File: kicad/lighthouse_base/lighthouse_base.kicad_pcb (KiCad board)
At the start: 2 copper layers, 0 parts

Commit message: started with pcb lighthouse_base
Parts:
- added BT1: Battery_Cell, Connector_PinHeader_2.54mm:PinHeader_1x02_P2.54mm_Vertical, F.Cu at (41.6, 130.1)
- added BT2: Keystone 3002, Battery:BatteryHolder_Keystone_3002_1x2032, F.Cu at (146.0, 62.2)
- added C1: 10uF, Capacitor_SMD:C_0805_2012Metric_Pad1.18x1.45mm_HandSolder, F.Cu at (66.6, 78.8)
- added C10: 100nF, Capacitor_SMD:C_0603_1608Metric_Pad1.08x0.95mm_HandSolder, F.Cu at (88.0, 79.6)
- added C11: 100nF, Capacitor_SMD:C_0603_1608Metric_Pad1.08x0.95mm_HandSolder, F.Cu at (88.0, 81.4)
- added C12: 10uF, Capacitor_SMD:C_0805_2012Metric_Pad1.18x1.45mm_HandSolder, F.Cu at (97.8, 102.2)
- added C13: 100nF, Capacitor_SMD:C_0603_1608Metric_Pad1.08x0.95mm_HandSolder, F.Cu at (103.1, 102.2)
- added C14: 100nF, Capacitor_SMD:C_0603_1608Metric_Pad1.08x0.95mm_HandSolder, F.Cu at (114.7, 79.8)
- added C2: 10uF, Capacitor_SMD:C_0805_2012Metric_Pad1.18x1.45mm_HandSolder, F.Cu at (74.1, 82.9)
- added C3: 10uF, Capacitor_SMD:C_0805_2012Metric_Pad1.18x1.45mm_HandSolder, F.Cu at (54.9, 125.2)
- added C4: 10uF, Capacitor_SMD:C_0805_2012Metric_Pad1.18x1.45mm_HandSolder, F.Cu at (73.4, 140.1)
- added C5: 10uF, Capacitor_SMD:C_0805_2012Metric_Pad1.18x1.45mm_HandSolder, F.Cu at (52.5, 108.3)
- added C6: 10nF, Capacitor_SMD:C_0603_1608Metric_Pad1.08x0.95mm_HandSolder, F.Cu at (64.2, 139.4)
- added C7: 10uF, Capacitor_SMD:C_0603_1608Metric_Pad1.08x0.95mm_HandSolder, F.Cu at (88.0, 74.4)
- added C8: 100nF, Capacitor_SMD:C_0603_1608Metric_Pad1.08x0.95mm_HandSolder, F.Cu at (88.0, 76.1)
- added C9: 100nF, Capacitor_SMD:C_0603_1608Metric_Pad1.08x0.95mm_HandSolder, F.Cu at (88.0, 77.9)
- added D1: B130-13-F, Diode_SMD:D_SMA_Handsoldering, F.Cu at (73.9, 89.9)
- added D2: DF2S16FS, Diode_SMD:D_SOD-523, F.Cu at (54.8, 86.0)
- added D3: B130-13-F, Diode_SMD:D_SMA_Handsoldering, F.Cu at (57.7, 103.3)
- added D4: PRTR5V0U2X, Package_TO_SOT_SMD:SOT-143, F.Cu at (56.9, 97.4)
- added D5: PMEG4002EJ, Diode_SMD:D_SOD-323F, F.Cu at (127.3, 63.4)
- added J1: Barrel_Jack_Switch, Connector_BarrelJack:BarrelJack_CUI_PJ-063AH_Horizontal, F.Cu at (52.4, 85.5)
- added J2: USB_C_Receptacle_USB2.0_14P, Connector_USB:USB_C_Receptacle_GCT_USB4110, F.Cu at (43.7, 99.3)
- added J3: Conn_01x07, Connector_PinHeader_1.27mm:PinHeader_1x07_P1.27mm_Vertical, F.Cu at (114.5, 112.3)
- added J4: Conn_01x12, Connector_Molex:Molex_Picoflex_90325-0012_2x06_P1.27mm_Vertical, F.Cu at (66.8, 110.6)
- added J5: Conn_01x12, Connector_Molex:Molex_Picoflex_90325-0012_2x06_P1.27mm_Vertical, F.Cu at (71.2, 54.9)
- added J6: Conn_01x06, Connector_Molex:Molex_Picoflex_90325-0006_2x03_P1.27mm_Vertical, F.Cu at (119.5, 54.4)
- added J7: Conn_01x02, Connector_PinHeader_2.54mm:PinHeader_1x02_P2.54mm_Vertical, F.Cu at (53.0, 51.3)
- added J8: Conn_01x05, Connector_PinHeader_1.27mm:PinHeader_1x05_P1.27mm_Vertical, F.Cu at (160.1, 70.2)
- added JP1: Jumper_3_Bridged12, Jumper:SolderJumper-3_P1.3mm_Bridged2Bar12_RoundedPad1.0x1.5mm, F.Cu at (46.5, 68.3)
- added Q1: DMP3099L, Package_TO_SOT_SMD:SOT-23-3, F.Cu at (57.6, 85.7)
- added R1: 1M, Resistor_SMD:R_0603_1608Metric_Pad0.98x0.95mm_HandSolder, F.Cu at (64.2, 142.9)
- added R10: 0R, Resistor_SMD:R_0603_1608Metric_Pad0.98x0.95mm_HandSolder, F.Cu at (96.0, 89.2)
- added R11: 1M, Resistor_SMD:R_0603_1608Metric_Pad0.98x0.95mm_HandSolder, F.Cu at (98.5, 89.2)
- added R12: 1M, Resistor_SMD:R_0603_1608Metric_Pad0.98x0.95mm_HandSolder, F.Cu at (101.0, 89.2)
- added R13: 4k7, Resistor_SMD:R_0603_1608Metric_Pad0.98x0.95mm_HandSolder, F.Cu at (107.0, 77.1)
- added R14: 4k7, Resistor_SMD:R_0603_1608Metric_Pad0.98x0.95mm_HandSolder, F.Cu at (107.0, 79.6)
- added R15: 10k, Resistor_SMD:R_0603_1608Metric_Pad0.98x0.95mm_HandSolder, F.Cu at (91.2, 71.5)
- added R2: 10k, Resistor_SMD:R_0603_1608Metric_Pad0.98x0.95mm_HandSolder, F.Cu at (59.5, 121.4)
- added R3: 22R, Resistor_SMD:R_0603_1608Metric_Pad0.98x0.95mm_HandSolder, F.Cu at (66.9, 96.6)
- added R4: 22R, Resistor_SMD:R_0603_1608Metric_Pad0.98x0.95mm_HandSolder, F.Cu at (66.9, 99.2)
- added R5: 5k1, Resistor_SMD:R_0603_1608Metric_Pad0.98x0.95mm_HandSolder, F.Cu at (62.4, 96.6)
- added R6: 5k1, Resistor_SMD:R_0603_1608Metric_Pad0.98x0.95mm_HandSolder, F.Cu at (62.4, 99.1)
- added R7: 0R, Resistor_SMD:R_0603_1608Metric_Pad0.98x0.95mm_HandSolder, F.Cu at (62.4, 73.2)
- added R8: 0R, Resistor_SMD:R_0603_1608Metric_Pad0.98x0.95mm_HandSolder, F.Cu at (62.4, 75.7)
- added R9: 0R, Resistor_SMD:R_0603_1608Metric_Pad0.98x0.95mm_HandSolder, F.Cu at (93.5, 89.2)
- added SW1: ~, lighthouse:PTS526, B.Cu at (130.4, 108.5)
- added TP1: TestPoint, TestPoint:TestPoint_Pad_D1.5mm, F.Cu at (101.7, 33.5)
- added TP10: TestPoint, TestPoint:TestPoint_Pad_D1.5mm, F.Cu at (108.8, 30.0)
- added TP11: TestPoint, TestPoint:TestPoint_Pad_D1.5mm, F.Cu at (112.3, 30.0)
- added TP12: TestPoint, TestPoint:TestPoint_Pad_D1.5mm, F.Cu at (115.9, 30.0)
- added TP13: TestPoint, TestPoint:TestPoint_Pad_D1.5mm, F.Cu at (119.4, 30.0)
- added TP14: TestPoint, TestPoint:TestPoint_Pad_D1.5mm, F.Cu at (101.7, 26.4)
- added TP15: TestPoint, TestPoint:TestPoint_Pad_D1.5mm, F.Cu at (105.2, 26.4)
- added TP16: TestPoint, TestPoint:TestPoint_Pad_D1.5mm, F.Cu at (108.8, 26.4)
- added TP17: TestPoint, TestPoint:TestPoint_Pad_D1.5mm, F.Cu at (112.3, 26.4)
- added TP18: TestPoint, TestPoint:TestPoint_Pad_D1.5mm, F.Cu at (115.9, 26.4)
- added TP19: TestPoint, TestPoint:TestPoint_Pad_D1.5mm, F.Cu at (119.4, 26.4)
- added TP2: TestPoint, TestPoint:TestPoint_Pad_D1.5mm, F.Cu at (105.2, 33.5)
- added TP20: TestPoint, TestPoint:TestPoint_Pad_D1.5mm, F.Cu at (125.4, 22.6)
- added TP21: TestPoint, TestPoint:TestPoint_Pad_D1.5mm, F.Cu at (125.4, 26.1)
- added TP22: TestPoint, TestPoint:TestPoint_Pad_D1.5mm, F.Cu at (125.4, 29.7)
- added TP23: TestPoint, TestPoint:TestPoint_Pad_D1.5mm, F.Cu at (125.4, 33.2)
- added TP24: TestPoint, TestPoint:TestPoint_Pad_D1.5mm, F.Cu at (125.4, 36.8)
- added TP3: TestPoint, TestPoint:TestPoint_Pad_D1.5mm, F.Cu at (108.8, 33.5)
- added TP4: TestPoint, TestPoint:TestPoint_Pad_D1.5mm, F.Cu at (112.3, 33.5)
- added TP5: TestPoint, TestPoint:TestPoint_Pad_D1.5mm, F.Cu at (115.9, 33.5)
- added TP7: TestPoint, TestPoint:TestPoint_Pad_D1.5mm, F.Cu at (119.4, 33.5)
- added TP8: TestPoint, TestPoint:TestPoint_Pad_D1.5mm, F.Cu at (101.7, 30.0)
- added TP9: TestPoint, TestPoint:TestPoint_Pad_D1.5mm, F.Cu at (105.2, 30.0)
- added U1: R-78E5.0-1.0, Converter_DCDC:Converter_DCDC_RECOM_R-78E-0.5_THT, F.Cu at (63.4, 87.3)
- added U2: MCP73831-2-OT, Package_TO_SOT_SMD:SOT-23-5, F.Cu at (64.3, 120.1)
- added U3: TLV75533PDBV, Package_TO_SOT_SMD:SOT-23-5, F.Cu at (70.2, 140.0)
- added U4: MCP111T-xxxE_TT, Package_TO_SOT_SMD:SOT-23-3, F.Cu at (60.7, 141.5)
- added U5: STM32L412R8Tx, Package_QFP:LQFP-64_10x10mm_P0.5mm, F.Cu at (97.7, 79.3)
- added U6: AT25SF081-SSHD-X, Package_SO:SOIC-8_3.9x4.9mm_P1.27mm, F.Cu at (96.7, 96.6)
- added U7: RV-3028-C7, Package_SON:MicroCrystal_C7_SON-8_1.5x3.2mm_P0.9mm, F.Cu at (111.0, 79.4)
- added U8: ~, lighthouse:DFPlayer_Mini-TF-16P, F.Cu at (50.1, 66.8)
- added U9: ~, lighthouse:BC805M, F.Cu at (158.1, 79.0)
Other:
- board text added: "Backlight"
- board text added: "Buttons"
- board text added: "Front Display"

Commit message: lighthouse base rev 1 done
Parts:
- removed TP19, TP20, TP5, TP7, TP8, TP9: TestPoint, TestPoint:TestPoint_Pad_D1.5mm
- added J10: Conn_01x07, Connector_PinHeader_2.54mm:PinHeader_1x07_P2.54mm_Vertical, F.Cu at (76.8, 109.0)
- added J9: Conn_01x04, Connector_PinHeader_2.54mm:PinHeader_1x04_P2.54mm_Vertical, F.Cu at (76.8, 112.0)
- C7: footprint Capacitor_SMD:C_0603_1608Metric_Pad1.08x0.95mm_HandSolder -> Capacitor_SMD:C_0805_2012Metric_Pad1.18x1.45mm_HandSolder
- TP1, TP10, TP11, TP12, TP13, TP14, TP15, TP16, TP17, TP18, TP2, TP21, TP22, TP23, TP24, TP3, TP4: footprint TestPoint:TestPoint_Pad_D1.5mm -> TestPoint:TestPoint_Pad_D1.0mm
- moved J8 66.2 mm to (109.6, 113.0)
- moved TP21 63.0 mm to (100.9, 84.1)
- moved TP22 56.9 mm to (103.4, 82.2)
- moved TP16 53.9 mm to (83.1, 73.8)
- moved TP13 53.8 mm to (87.3, 73.2)
- moved TP23 52.5 mm to (105.4, 81.7)
- moved TP14 49.6 mm to (85.1, 73.2)
- moved U4 49.0 mm to (74.8, 94.6)
- moved TP18 47.8 mm to (91.8, 67.7)
- moved TP2 47.7 mm to (83.1, 75.8)
- moved C4 47.6 mm to (83.6, 93.6)
- moved U3 47.6 mm to (80.5, 93.5)
- moved TP24 47.3 mm to (105.4, 79.6)
- moved R1 47.0 mm to (74.8, 97.1), turned to 0 degrees
- moved C6 46.7 mm to (77.6, 94.6)
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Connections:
- net SPI_SCLK renamed SPI1_SCLK
- U5 pad 11: Net-(U5-PC3) -> unconnected-(U5-PC3-Pad11)
- U5 pad 29: Net-(U5-PB10) -> unconnected-(U5-PB10-Pad29)
- U5 pad 30: Net-(U5-PB11) -> unconnected-(U5-PB11-Pad30)
- U5 pad 40: Net-(U5-PC9) -> unconnected-(U5-PC9-Pad40)
- U5 pad 41: Net-(U5-PA8) -> ~{SPI1_CS1}
- U5 pad 50: Net-(U5-PA15) -> ~{SPI1_CS2}
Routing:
- net +3.3V: track 0.00 -> 338.6 mm, vias 0 -> 9
- net I2C1_SDA: track 0.00 -> 166.9 mm, vias 0 -> 3
- net I2C1_SCL: track 0.00 -> 163.8 mm, vias 0 -> 4
- net ~{IS_INTB}: track 0.00 -> 129.3 mm, vias 0 -> 3
- net ~{IS_SDB}: track 0.00 -> 126.9 mm, vias 0 -> 3
- net GND: track 0.00 -> 125.9 mm, vias 0 -> 15
- net +5V: track 0.00 -> 83.4 mm, vias 0 -> 2
- net +12V: track 0.00 -> 70.2 mm, vias 0 -> 1
- net ~{STM_RST}: track 0.00 -> 67.9 mm, vias 0 -> 3
- net USB_D-: track 0.00 -> 64.2 mm, vias 0 -> 2
- net USB_D+: track 0.00 -> 64.2 mm, vias 0 -> 2
- net BTN1: track 0.00 -> 53.7 mm, vias 0 -> 2
- net WHITE_PWM2: track 0.00 -> 52.5 mm, vias 0 -> 2
- net ~{SPI1_CS2}: track 0.00 -> 52.5 mm, vias 0 -> 2
- net Net-(BT2-+): track 0.00 -> 52.1 mm
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- added copper zone on In2.Cu, net GND
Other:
- board outline added: 90 x 66.3 mm
- copper layers 2 -> 4
- board text added: "lighthouse base rev1 MEgli 2024-11-06"

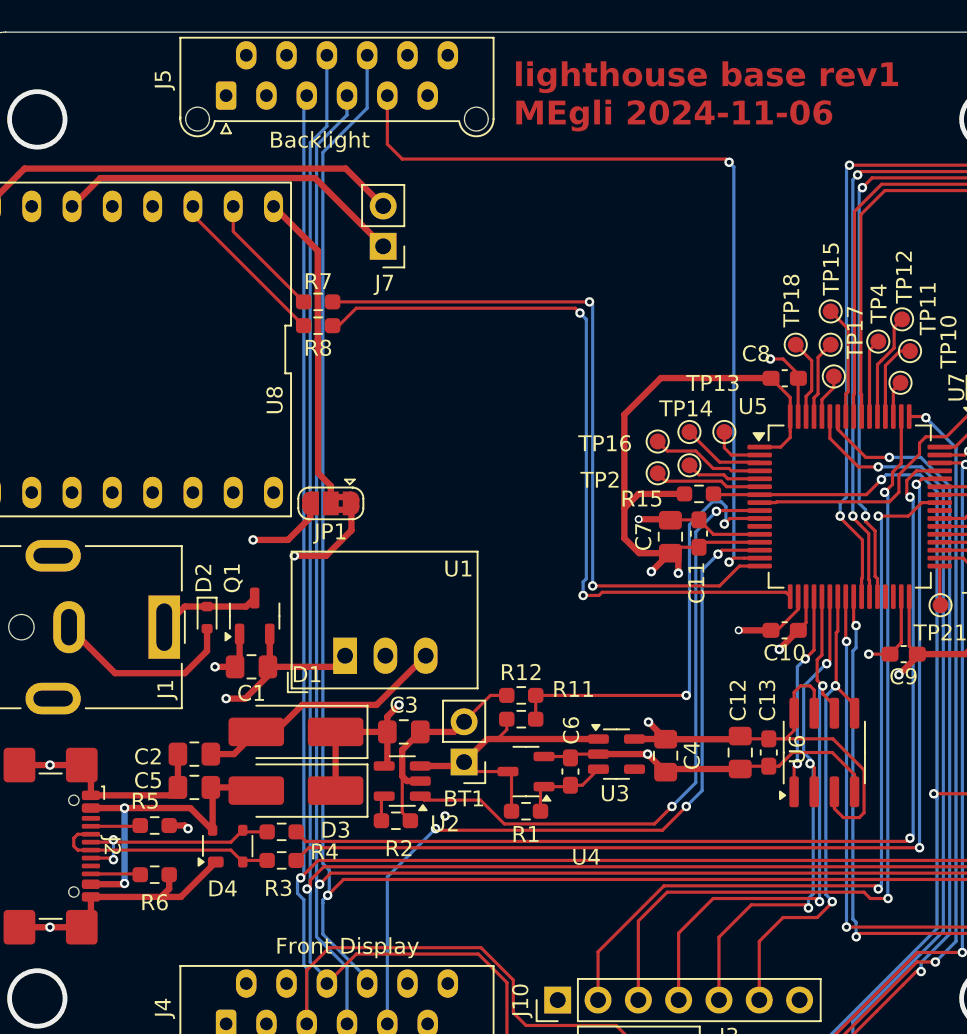
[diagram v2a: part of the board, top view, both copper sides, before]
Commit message: rev1: added 32 kHz XTAL, interrupt signals for VBUS + +5V, ... many more
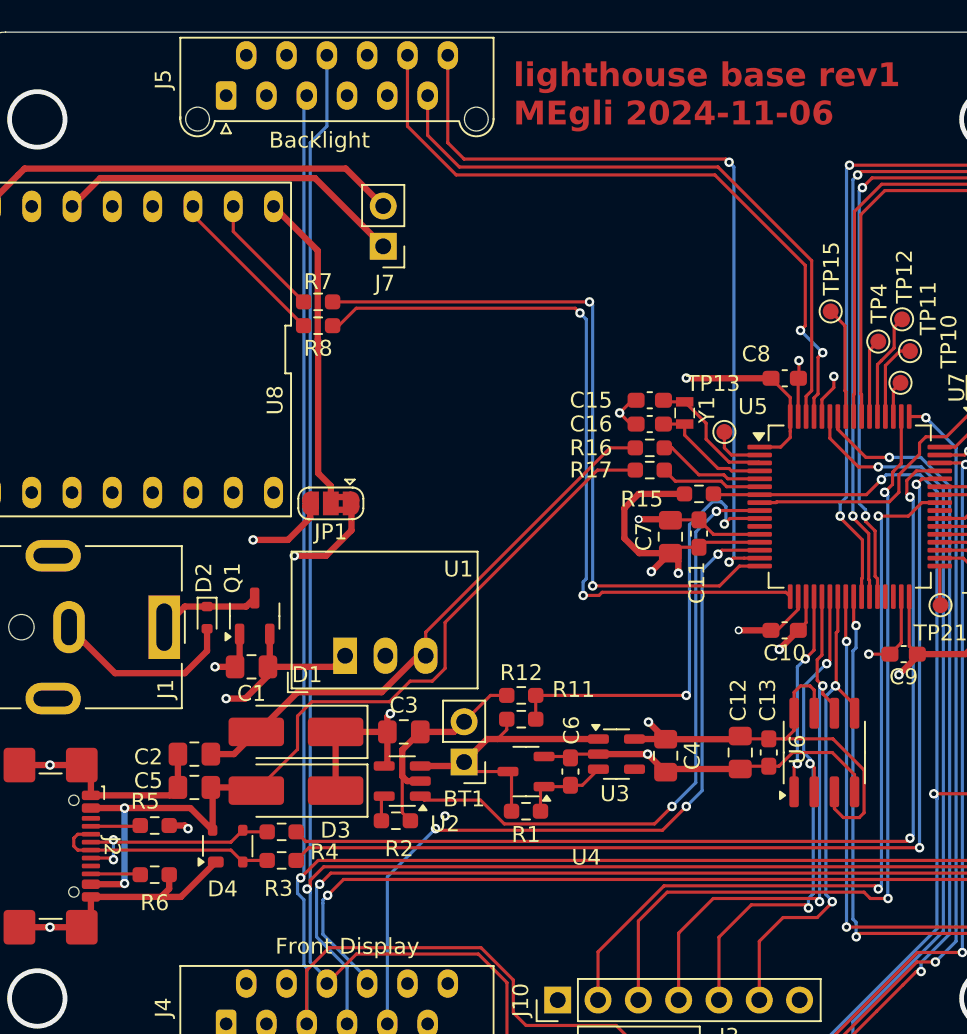
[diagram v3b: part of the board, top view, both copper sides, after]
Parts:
- removed TP1, TP14, TP16, TP17, TP18, TP2, TP3: TestPoint, TestPoint:TestPoint_Pad_D1.0mm
- added C15: 12.5pF, Capacitor_SMD:C_0603_1608Metric_Pad1.08x0.95mm_HandSolder, F.Cu at (82.6, 71.2)
- added C16: 12.5pF, Capacitor_SMD:C_0603_1608Metric_Pad1.08x0.95mm_HandSolder, F.Cu at (82.6, 72.7)
- added R16: 1k, Resistor_SMD:R_0603_1608Metric_Pad0.98x0.95mm_HandSolder, F.Cu at (82.6, 74.2)
- added R17: 1k, Resistor_SMD:R_0603_1608Metric_Pad0.98x0.95mm_HandSolder, F.Cu at (82.6, 75.6)
- added Y1: 9HT11-32.768KDZB-T, Lighthouse1:9HT1132768KDZBT, F.Cu at (84.8, 72.0)
- U5: value STM32L412R8Tx -> STM32L412RBTx
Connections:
- net Net-(D1-A) renamed +5VA
- J4 pad 7: ~{IS_SDB} -> ~{IS_SDB1}
- J4 pad 8: ~{IS_INTB} -> ~{IS_INTB1}
- J5 pad 10: unconnected-(J5-Pin_10-Pad10) -> ~{IS_SDB2}
- J5 pad 11: unconnected-(J5-Pin_11-Pad11) -> ~{IS_INTB2}
- J5 pad 12: unconnected-(J5-Pin_12-Pad12) -> WHITE_PWM2
- J5 pad 7: ~{IS_SDB} -> unconnected-(J5-Pin_7-Pad7)
- J5 pad 8: ~{IS_INTB} -> unconnected-(J5-Pin_8-Pad8)
- J5 pad 9: WHITE_PWM2 -> unconnected-(J5-Pin_9-Pad9)
- U5 pad 37: ~{IS_SDB} -> ~{IS_SDB1}
- U5 pad 38: ~{IS_INTB} -> ~{IS_INTB1}
- U5 pad 60: Net-(U5-PH3) -> GND
- U5 pad 61: Net-(U5-PB8) -> ~{IS_SDB2}
- U5 pad 62: Net-(U5-PB9) -> ~{IS_INTB2}
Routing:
- net ~{IS_INTB}: track 129.3 -> 0.00 mm, vias 3 -> 0
- net ~{IS_SDB}: track 126.9 -> 0.00 mm, vias 3 -> 0
- net ~{IS_SDB1}: track 0.00 -> 76.2 mm, vias 0 -> 3
- net ~{IS_INTB1}: track 0.00 -> 75.1 mm, vias 0 -> 3
- net ~{IS_SDB2}: track 0.00 -> 43.6 mm, vias 0 -> 2
- net ~{IS_INTB2}: track 0.00 -> 39.9 mm
- net VBUS: track 20.9 -> 56.1 mm
- net +5VA: track 16.1 -> 35.6 mm
- net Net-(U5-PB9): track 5.09 -> 0.00 mm
- net Net-(U5-PB8): track 4.96 -> 0.00 mm
- net GND: track 125.9 -> 130.1 mm, vias 15 -> 17
- net Net-(U5-PC14): track 5.23 -> 8.28 mm
- net Net-(U5-PH3): track 2.84 -> 0.00 mm
- net Net-(U5-PH0): track 4.78 -> 6.82 mm
- net +3.3V: track 338.6 -> 340.4 mm, vias 9 -> 10
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
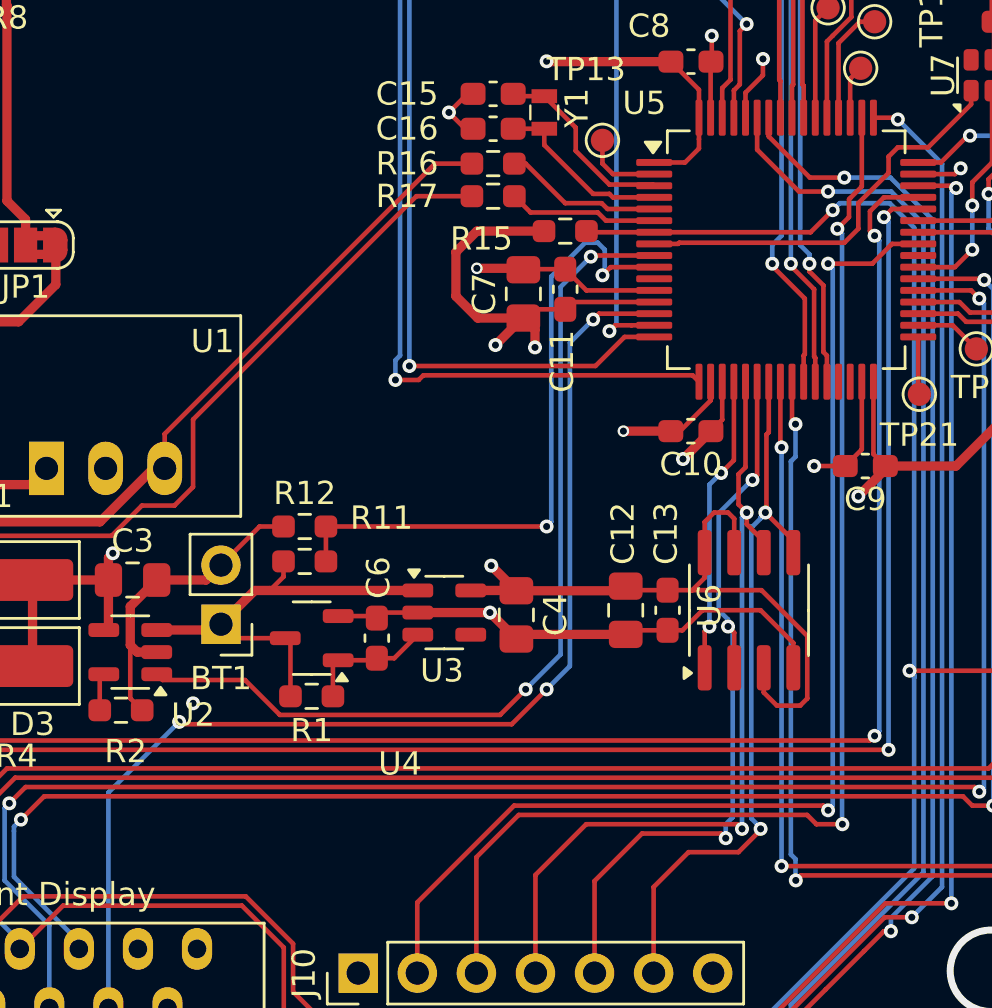
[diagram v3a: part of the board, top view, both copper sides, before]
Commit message: ordererd lighthouse display
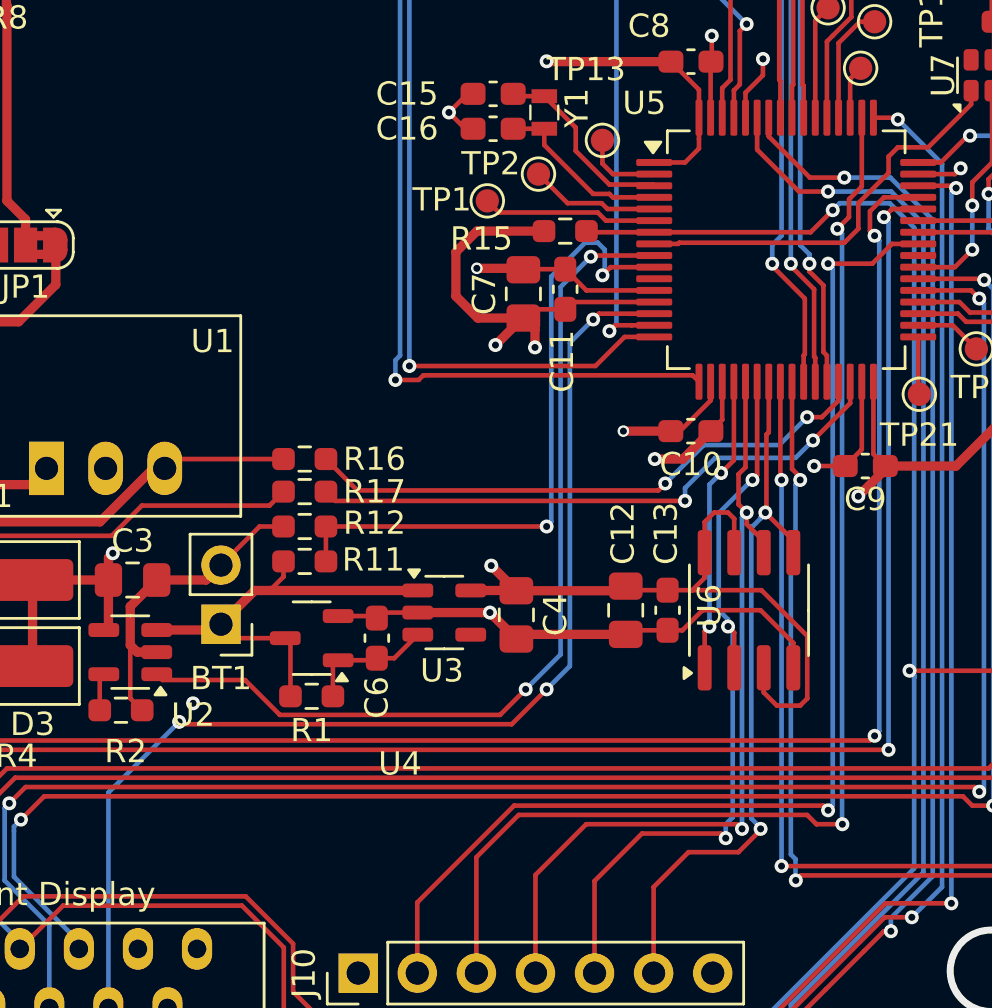
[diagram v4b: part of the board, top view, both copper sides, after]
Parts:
- added TP1: TestPoint, TestPoint:TestPoint_Pad_D1.0mm, F.Cu at (82.3, 75.8)
- added TP2: TestPoint, TestPoint:TestPoint_Pad_D1.0mm, F.Cu at (84.5, 74.7)
- moved R16 15.1 mm to (74.5, 86.9)
- moved R17 15.1 mm to (74.5, 88.3)
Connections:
- R16 pad 2: Net-(U5-PH0) -> Net-(U5-PB10)
- R17 pad 2: Net-(U5-PH1) -> Net-(U5-PB11)
- U5 pad 29: unconnected-(U5-PB10-Pad29) -> Net-(U5-PB10)
- U5 pad 30: unconnected-(U5-PB11-Pad30) -> Net-(U5-PB11)
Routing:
- net Net-(U5-PB11): track 0.00 -> 25.7 mm, vias 0 -> 2
- net Net-(U5-PB10): track 0.00 -> 25.0 mm, vias 0 -> 2
- net VBUS: track 56.1 -> 41.0 mm
- net +5VA: track 35.6 -> 21.4 mm
- net +3.3V: track 340.4 -> 342.0 mm
- net Net-(U5-PH0): track 6.82 -> 5.60 mm
- net Net-(U5-PH1): track 6.45 -> 7.53 mm
